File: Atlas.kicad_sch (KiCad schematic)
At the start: 46 parts, among them J101 BATT, J102 GND, J104 Conn_01x08_MountingPin, U101 INA186A2, U102 LMR51420YDDCR, U103 TLV76733DRVR

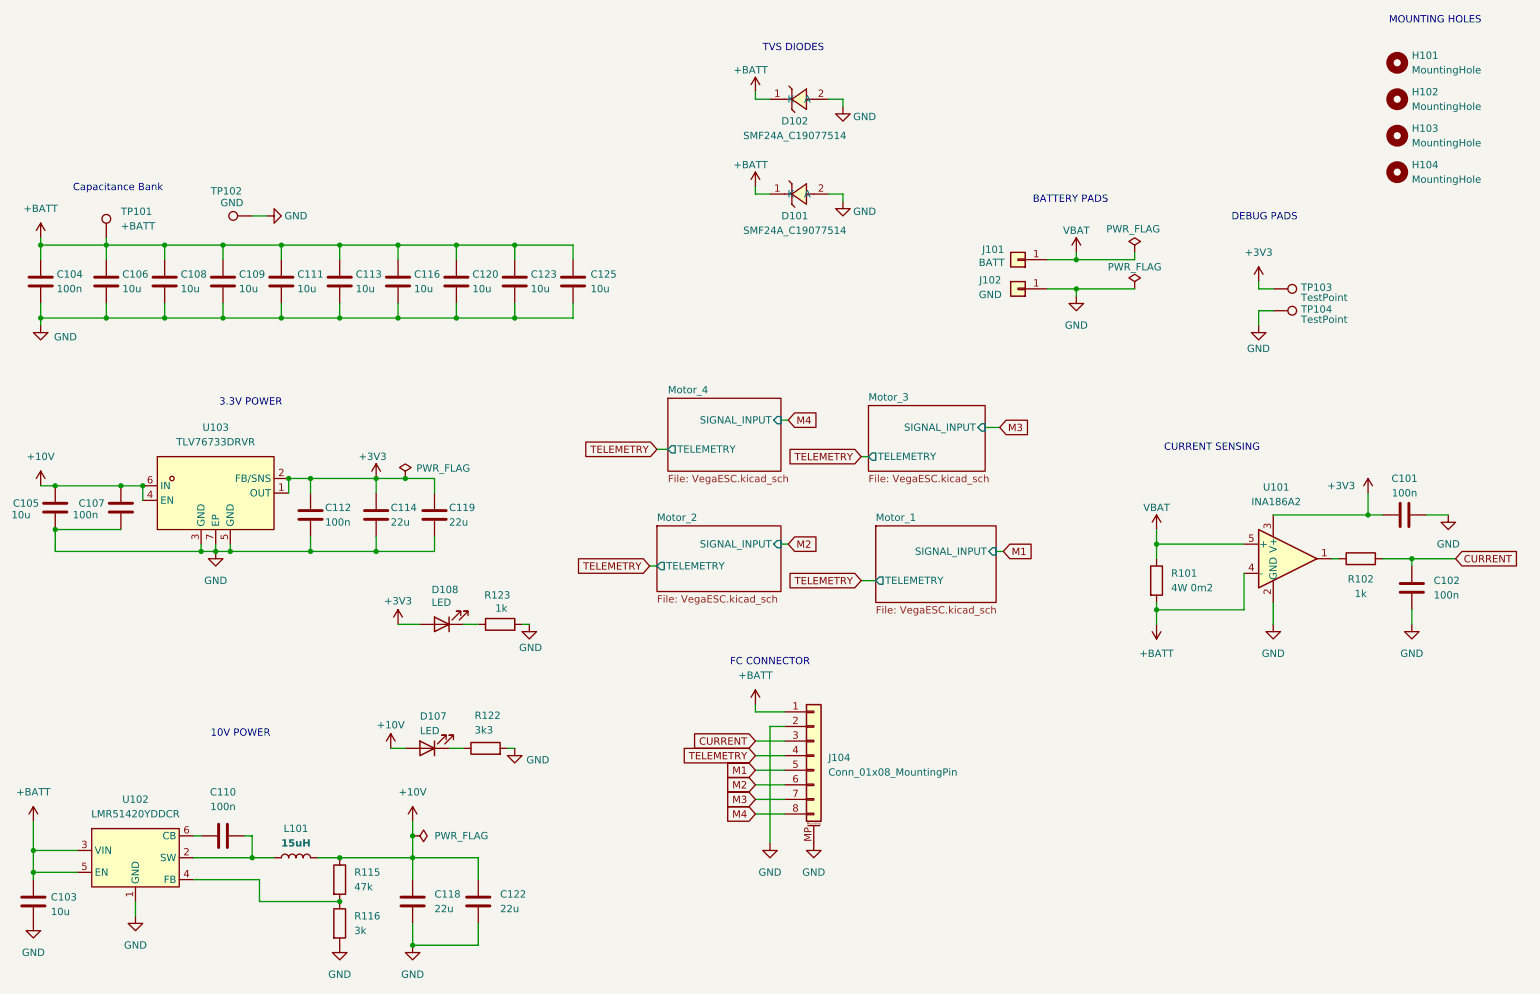
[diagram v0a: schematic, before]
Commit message: fix: assign standard footprints to all schematic components and resolve 189 missing footprint warnings
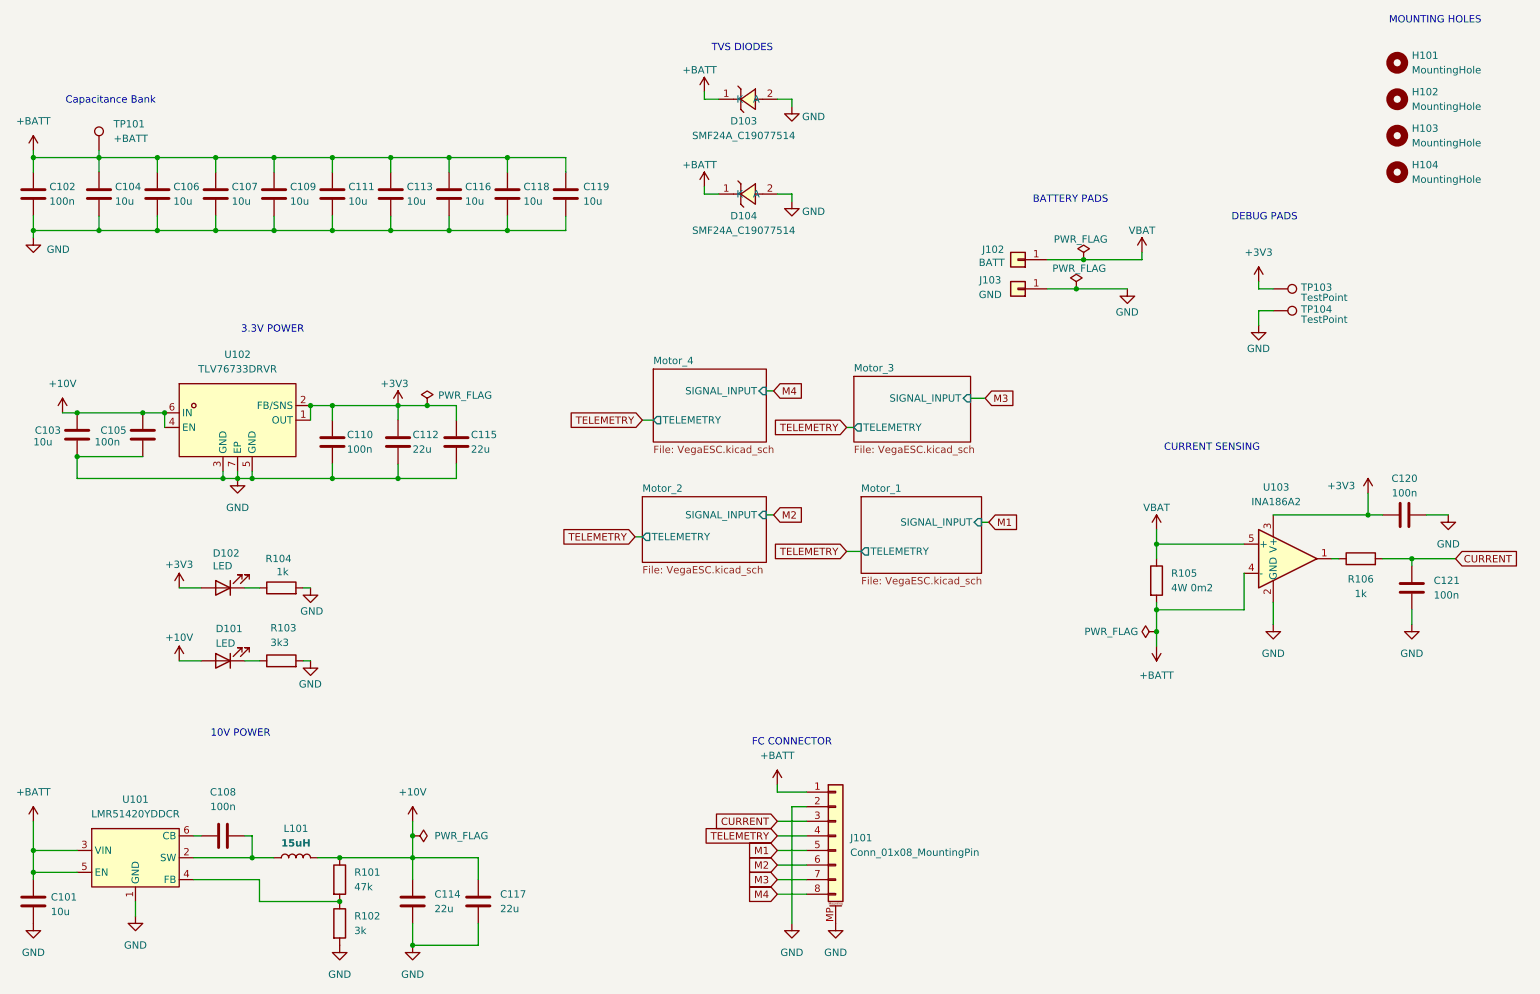
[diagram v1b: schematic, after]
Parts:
- removed TP102: GND, symbol Connector:TestPoint
- C102: renamed from C104; footprint (none) -> Capacitor_SMD:C_0603_1608Metric
- C103: renamed from C105; footprint (none) -> Capacitor_SMD:C_1206_3216Metric
- C104: renamed from C106; footprint (none) -> Capacitor_SMD:C_1206_3216Metric
- C105: renamed from C107; footprint (none) -> Capacitor_SMD:C_0402_1005Metric
- C106: renamed from C108; footprint (none) -> Capacitor_SMD:C_1206_3216Metric
- C107: renamed from C109; footprint (none) -> Capacitor_SMD:C_1206_3216Metric
- C109: renamed from C111; footprint (none) -> Capacitor_SMD:C_1206_3216Metric
- C110: renamed from C112; footprint (none) -> Capacitor_SMD:C_0402_1005Metric
- C111: renamed from C113; footprint (none) -> Capacitor_SMD:C_1206_3216Metric
- C112: renamed from C114; footprint (none) -> Capacitor_SMD:C_0805_2012Metric
- C113: renamed from C116; footprint (none) -> Capacitor_SMD:C_1206_3216Metric
- C115: renamed from C119; footprint (none) -> Capacitor_SMD:C_0805_2012Metric
- C116: renamed from C120; footprint (none) -> Capacitor_SMD:C_1206_3216Metric
- C118: renamed from C123; footprint (none) -> Capacitor_SMD:C_1206_3216Metric
- C119: renamed from C125; footprint (none) -> Capacitor_SMD:C_1206_3216Metric
- C120: renamed from C101; footprint (none) -> Capacitor_SMD:C_0603_1608Metric
- C121: renamed from C102; footprint (none) -> Capacitor_SMD:C_0603_1608Metric
- R103: renamed from R122; footprint (none) -> Resistor_SMD:R_0603_1608Metric
- R104: renamed from R123; footprint (none) -> Resistor_SMD:R_0603_1608Metric
- R105: renamed from R101; footprint (none) -> easyeda2kicad:R2725
- R106: renamed from R102; footprint (none) -> Resistor_SMD:R_0603_1608Metric
- TP101: footprint (none) -> TestPoint:TestPoint_Pad_4.0x4.0mm
- TP103, TP104: footprint (none) -> TestPoint:TestPoint_Pad_D1.0mm
- renumbered C103 to C101, C110 to C108, C118 to C114, C122 to C117, D107 to D101, D108 to D102, D102 to D103, D101 to D104, J104 to J101, J101 to J102, J102 to J103, R115 to R101, R116 to R102, U102 to U101, U103 to U102, U101 to U103
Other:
- moved on the sheet: C102, C103, C104, C105, C106, C107, C109, C110, C111, C112, C113, C115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

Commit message: update: add standard lcsc property to TVS diodes and regenerate BOM
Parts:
- D103, D104: lcsc (none) -> C19077514
- J101: MPN (none) -> SM08B-SRSS-TB(LF)(SN); Manufacturer (none) -> JST; lcsc (none) -> C160401
- R105: MPN (none) -> HOLR2725D-4W-0.2MR-1%
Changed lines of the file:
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@@
 			)
 		)
-		(property "MPN" ""
+		(property "MPN" "HOLR2725D-4W-0.2MR-1%"
 			(at 167.64 -60.96 0)
 			(hide yes)
@@
 			)
 		)
+		(property "lcsc" "C19077514" (at 0 0 0)
+			(effects
+				(font
+					(size 1.27 1.27)
+				)
+				(hide yes)
+			)
+		)
 		(pin "2"
 		)
@@
 			)
 		)
+		(property "lcsc" "C19077514" (at 0 0 0)
+			(effects
+				(font
+					(size 1.27 1.27)
+				)
+				(hide yes)
+			)
+		)
 		(pin "2"
 		)
@@
 			)
 		)
-		(property "Datasheet" ""
+		(property "Datasheet" "https://datasheet.lcsc.com/datasheet/pdf/2304141430_JST-SM08B-SRSS-TB-LF-SN_C160401.pdf"
 			(at 161.29 167.64 0)
 			(hide yes)
@@
 			)
 		)
+		(property "lcsc" "C160401" (at 0 0 0)
+			(effects
+				(font
+					(size 1.27 1.27)
+				)
+				(hide yes)
+			)
+		)
+		(property "Manufacturer" "JST" (at 0 0 0)
+			(effects
+				(font
+					(size 1.27 1.27)
+				)
+				(hide yes)
+			)
+		)
+		(property "MPN" "SM08B-SRSS-TB(LF)(SN)" (at 0 0 0)
+			(effects
+				(font
+					(size 1.27 1.27)
+				)
+				(hide yes)
+			)
+		)
